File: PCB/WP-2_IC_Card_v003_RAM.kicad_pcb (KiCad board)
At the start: 2 copper layers, 14.5 x 48.5 mm, 8 parts, among them J1 Conn_01x38_Female, U1 SRAM 128Kx8 5v Parallel, U2 SRAM 128Kx8 5v Parallel

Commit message: v003 RAM and ROM versions
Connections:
- J1 pad 17: /A17 -> (no net)
- U1 pad 9: /A17 -> (no net)
- U2 pad 9: /A17 -> (no net)
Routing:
- net /A17: track 20.5 -> 0.00 mm, vias 2 -> 0
- net GND: vias 7 -> 8
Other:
- board text added: "TANDY WP-2 128K RAM"
- board text added: "v003_RAM"
- board text removed: "TANDY WP-2 IC CARD"
- board text removed: "[ ]128K"
- board text removed: "[ ]256K"
- board text removed: "[ ]RAM"
- board text removed: "[ ]ROM"
- board text removed: "v003"

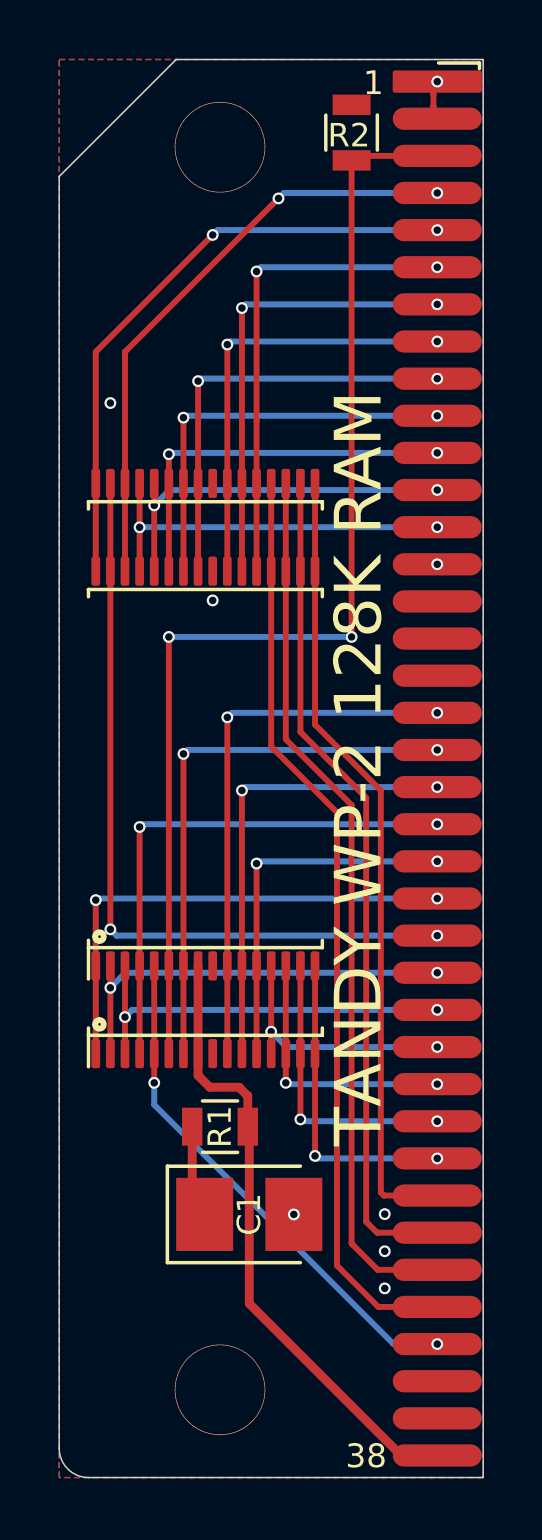
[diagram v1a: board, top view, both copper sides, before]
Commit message: v003_RAM, v003_ROM, ROM programming adapter, v004_RAM_B
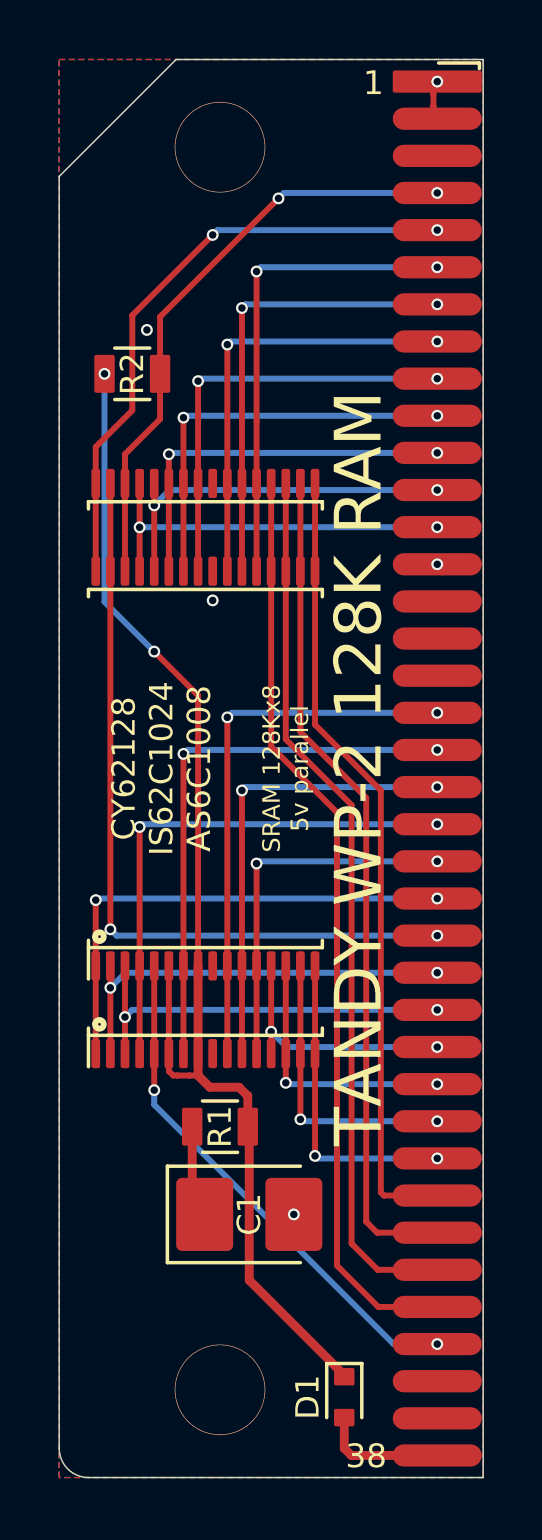
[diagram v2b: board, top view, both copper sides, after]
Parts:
- added D1: 1SS389, 0_LOCAL:D_SOD-523, F.Cu at (154.0, 121.2)
- added NT2: Net-Tie_2, 0_LOCAL:Net_Tie_2p_8mil, F.Cu at (148.5, 110.2)
- R1: value 4.7K -> 15K
- R2: value 47K -> 15K
- moved R2 11.1 mm to (146.8, 86.2), turned to 0 degrees
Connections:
- J1 pad 3: /CE2 -> (no net)
- J1 pad 38: VDD -> VBUS
- R1 pad 1: VDD -> VMEM
- R2 pad 1: GND -> VMEM
- R2 pad 2: /CE2 -> /~CE1
- U1 pad 8: VDD -> VMEM
- U2 pad 8: VDD -> VMEM
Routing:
- net VMEM: track 0.00 -> 38.6 mm, vias 0 -> 2
- net /CE2: track 39.8 -> 3.96 mm, vias 2 -> 0
- net VDD: track 21.4 -> 0.00 mm
- net VBUS: track 0.00 -> 4.33 mm
- net GND: track 0.99 -> 0.49 mm, vias 8 -> 5
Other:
- board text added: "CY62128 IS62C1024 AS6C1008"
- board text added: "SRAM 128Kx8 5v parallel"
